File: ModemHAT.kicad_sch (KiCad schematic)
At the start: 99 parts, among them J1 RJ11, J2 2x20 0.1" Stacking Header, J3 8R, Q1 NPN 300V 0.5A, Q2 PNP 300V 0.5A, Q3 NPN 300V 0.5A, Q4 NPN 80V 330mW, Q5 NPN 80V 330mW, SW1 SW_SPDT, U1 Si2457-D-FT, U2 Si3018-F-GS, U3 74LVC541, U4 LM4819, U5 24LC32, U6 25LC320, Y1 32.768kHz 25ppm

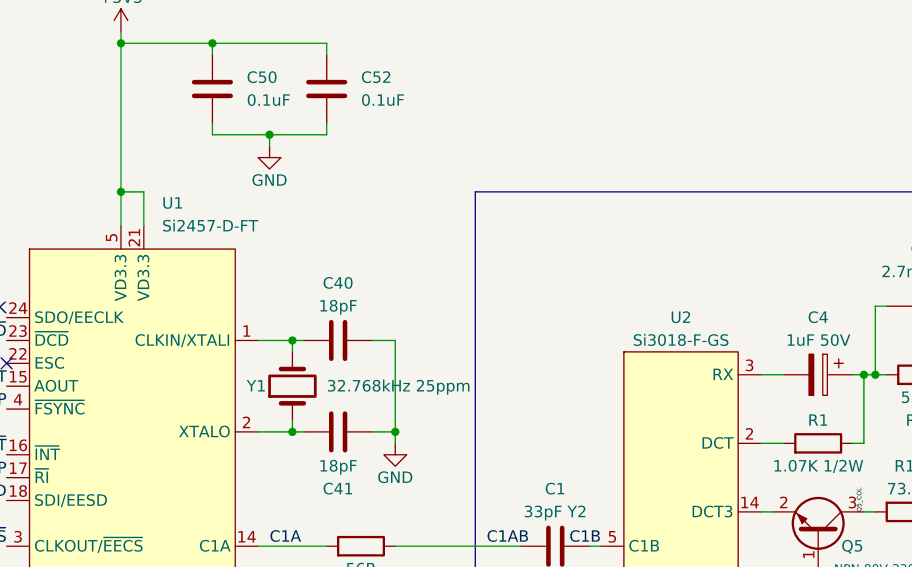
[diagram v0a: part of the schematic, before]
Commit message: added more mfg part numbers
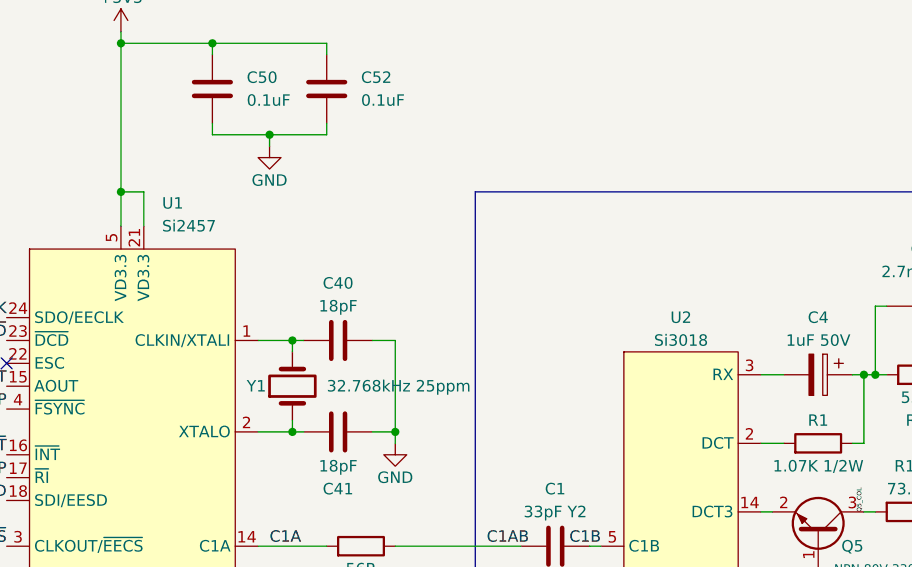
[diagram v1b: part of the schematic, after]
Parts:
- C3: MPN (none) -> GRM21BR72E103KW03L
- C8, C9: MPN (none) -> 502R29W681KV3E-****-SC
- D1: MPN MB4S -> MB4S-TP
- H1, H2, H3, H4: now left out of the parts list
- J1: MPN (none) -> 54601-906001WPLF
- SW1: MPN (none) -> JS102011SAQN
- U1: value Si2457-D-FT -> Si2457; MPN (none) -> Si2457-D-FT
- U2: value Si3018-F-GS -> Si3018; MPN (none) -> Si3018-F-GS
- U3: MPN (none) -> 74LVC541ABQ,115
- U4: MPN (none) -> LM4819MX/NOPB
- U5: MPN (none) -> CAT24C32YI-GT3
- U6: MPN (none) -> 25LC320AT-I/ST
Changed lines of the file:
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@@
+      (effects (font (size 1.27 1.27)) hide)
+    )
+    (property "MPN" "GRM21BR72E103KW03L" (id 4) (at 234.95 105.41 0)
       (effects (font (size 1.27 1.27)) hide)
     )
@@
   )
   (symbol (lib_id "Mechanical:MountingHole") (at 256.54 236.22 0) (unit 1)
-    (in_bom yes) (on_board yes) (fields_autoplaced)
+    (in_bom no) (on_board yes) (fields_autoplaced)
     (property "Reference" "H1" (id 0) (at 259.08 234.9499 0)
       (effects (font (size 1.27 1.27)) (justify left))
@@
   )
   (symbol (lib_id "Mechanical:MountingHole") (at 256.54 245.11 0) (unit 1)
-    (in_bom yes) (on_board yes) (fields_autoplaced)
+    (in_bom no) (on_board yes) (fields_autoplaced)
     (property "Reference" "H3" (id 0) (at 259.08 243.8399 0)
       (effects (font (size 1.27 1.27)) (justify left))
@@
     )
     (property "Datasheet" "~" (id 3) (at 262.89 142.24 0)
+      (effects (font (size 1.27 1.27)) hide)
+    )
+    (property "MPN" "502R29W681KV3E-****-SC" (id 4) (at 262.89 142.24 0)
       (effects (font (size 1.27 1.27)) hide)
     )
@@
     )
     (property "Datasheet" "~" (id 3) (at 298.45 90.805 90)
+      (effects (font (size 1.27 1.27)) hide)
+    )
+    (property "MPN" "54601-906001WPLF" (id 4) (at 298.45 90.17 0)
       (effects (font (size 1.27 1.27)) hide)
     )
@@
   )
   (symbol (lib_id "Graphic:Logo_Open_Hardware_Small") (at 397.51 261.62 0) (unit 1)
-    (in_bom yes) (on_board yes) (fields_autoplaced)
+    (in_bom no) (on_board yes) (fields_autoplaced)
     (property "Reference" "#LOGO1" (id 0) (at 397.51 254.635 0)
       (effects (font (size 1.27 1.27)) hide)
@@
       (effects (font (size 1.27 1.27)) hide)
     )
-    (property "MPN" "MB4S" (id 4) (at 237.49 90.17 0)
+    (property "MPN" "MB4S-TP" (id 4) (at 237.49 90.17 0)
       (effects (font (size 1.27 1.27)) hide)
     )
@@
   )
   (symbol (lib_id "Mechanical:MountingHole") (at 267.97 245.11 0) (unit 1)
-    (in_bom yes) (on_board yes) (fields_autoplaced)
+    (in_bom no) (on_board yes) (fields_autoplaced)
     (property "Reference" "H4" (id 0) (at 270.51 243.8399 0)
       (effects (font (size 1.27 1.27)) (justify left))
@@
       (effects (font (size 1.27 1.27)) (justify left))
     )
-    (property "Value" "Si2457-D-FT" (id 1) (at 79.4894 58.42 0)
+    (property "Value" "Si2457" (id 1) (at 79.4894 58.42 0)
       (effects (font (size 1.27 1.27)) (justify left))
     )
@@
     )
     (property "Datasheet" "" (id 3) (at 77.47 90.17 0)
+      (effects (font (size 1.27 1.27)) hide)
+    )
+    (property "MPN" "Si2457-D-FT" (id 4) (at 76.2 90.17 0)
       (effects (font (size 1.27 1.27)) hide)
     )
@@
       (effects (font (size 1.27 1.27)) hide)
     )
+    (property "MPN" "JS102011SAQN" (id 4) (at 195.58 243.84 0)
+      (effects (font (size 1.27 1.27)) hide)
+    )
     (pin "1")
     (pin "2")
@@
     )
     (property "Datasheet" "http://www.ti.com/lit/ds/symlink/lm4819.pdf" (id 3) (at 133.35 247.65 0)
+      (effects (font (size 1.27 1.27)) hide)
+    )
+    (property "MPN" "LM4819MX/NOPB" (id 4) (at 133.35 247.65 0)
       (effects (font (size 1.27 1.27)) hide)
     )
@@
     (in_bom yes) (on_board yes)
     (property "Reference" "U2" (id 0) (at 137.16 68.58 0))
-    (property "Value" "Si3018-F-GS" (id 1) (at 137.16 71.12 0))
+    (property "Value" "Si3018" (id 1) (at 137.16 71.12 0))
     (property "Footprint" "Package_SO:SOIC-16_3.9x9.9mm_P1.27mm" (id 2) (at 137.16 106.68 0)
       (effects (font (size 1.27 1.27)) hide)
     )
     (property "Datasheet" "" (id 3) (at 137.16 106.68 0)
+      (effects (font (size 1.27 1.27)) hide)
+    )
+    (property "MPN" "Si3018-F-GS" (id 4) (at 137.16 113.03 0)
       (effects (font (size 1.27 1.27)) hide)
     )
@@
   )
   (symbol (lib_id "Mechanical:MountingHole") (at 267.97 236.22 0) (unit 1)
-    (in_bom yes) (on_board yes) (fields_autoplaced)
+    (in_bom no) (on_board yes) (fields_autoplaced)
     (property "Reference" "H2" (id 0) (at 270.51 234.9499 0)
       (effects (font (size 1.27 1.27)) (justify left))
@@
     )
     (property "Datasheet" "~" (id 3) (at 269.24 142.24 0)
+      (effects (font (size 1.27 1.27)) hide)
+    )
+    (property "MPN" "502R29W681KV3E-****-SC" (id 4) (at 269.24 142.24 0)
       (effects (font (size 1.27 1.27)) hide)
     )
@@
       (effects (font (size 1.27 1.27)) hide)
     )
+    (property "MPN" "74LVC541ABQ,115" (id 4) (at 339.09 204.47 0)
+      (effects (font (size 1.27 1.27)) hide)
+    )
     (pin "1")
     (pin "10")
@@
       (effects (font (size 1.27 1.27)) hide)
     )
+    (property "MPN" "25LC320AT-I/ST" (id 4) (at 218.44 194.31 0)
+      (effects (font (size 1.27 1.27)) hide)
+    )
     (pin "1")
     (pin "2")
@@
       (effects (font (size 1.27 1.27)) hide)
     )
+    (property "MPN" "CAT24C32YI-GT3" (id 4) (at 361.95 128.27 0)
+      (effects (font (size 1.27 1.27)) hide)
+    )
     (pin "1")
     (pin "2")
@@
     )
     (path "/76561a30-8f21-41fc-a06c-445f9a92101b"
-      (reference "U1") (unit 1) (value "Si2457-D-FT") (footprint "Package_SO:TSSOP-24_4.4x7.8mm_P0.65mm")
+      (reference "U1") (unit 1) (value "Si2457") (footprint "Package_SO:TSSOP-24_4.4x7.8mm_P0.65mm")
     )
     (path "/9b33db79-b98e-4c51-8305-ed7f7bb70f13"
-      (reference "U2") (unit 1) (value "Si3018-F-GS") (footprint "Package_SO:SOIC-16_3.9x9.9mm_P1.27mm")
+      (reference "U2") (unit 1) (value "Si3018") (footprint "Package_SO:SOIC-16_3.9x9.9mm_P1.27mm")
     )
     (path "/f4f2738d-4efa-400b-bd93-c96242dafc30"

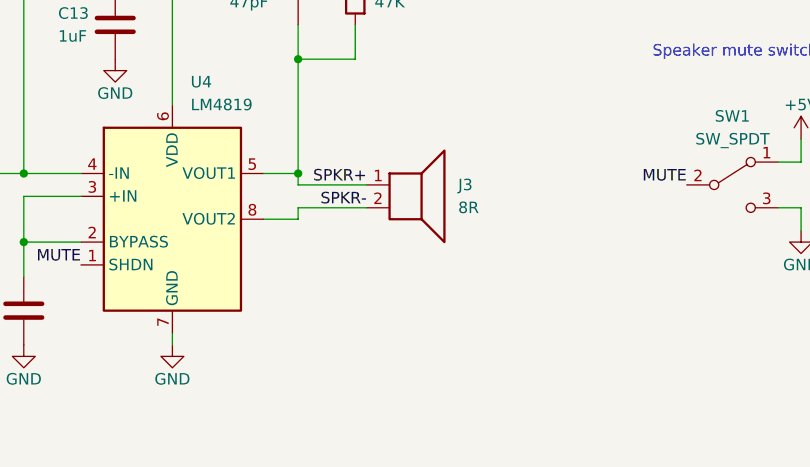
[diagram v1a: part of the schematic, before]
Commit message: audio circuit comments
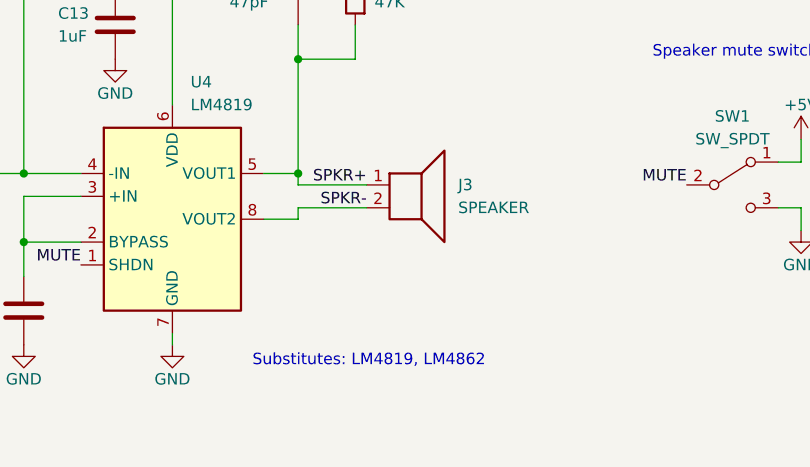
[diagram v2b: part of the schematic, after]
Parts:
- J3: value 8R -> SPEAKER
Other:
- note added: "Substitutes: LM4819, LM4862"
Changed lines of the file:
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@@
+    (effects (font (size 1.27 1.27)) (justify left bottom))
+  )
+  (text "Substitutes: LM4819, LM4862" (at 142.24 264.16 0)
     (effects (font (size 1.27 1.27)) (justify left bottom))
   )
@@
       (effects (font (size 1.27 1.27)) (justify left))
     )
-    (property "Value" "8R" (id 1) (at 165.1 246.3799 0)
+    (property "Value" "SPEAKER" (id 1) (at 165.1 246.3799 0)
       (effects (font (size 1.27 1.27)) (justify left))
     )
@@
     )
     (path "/6effeffe-d42d-4a4b-9f82-74cae02f5e28"
-      (reference "J3") (unit 1) (value "8R") (footprint "Connector_JST:JST_PH_B2B-PH-K_1x02_P2.00mm_Vertical")
+      (reference "J3") (unit 1) (value "SPEAKER") (footprint "Connector_JST:JST_PH_B2B-PH-K_1x02_P2.00mm_Vertical")
     )
     (path "/a1821338-ea80-47ff-948f-c44a9f05bfce"

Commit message: rev B
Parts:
- removed RN1, RN2: 470R, Resistor_SMD:R_Array_Concave_4x0603, symbol Device:R_Pack04_Split
- added LS1: Speaker, Buzzer_Beeper:Buzzer_15x7.5RM7.6, symbol Device:Speaker
- added R34, R35, R36, R37, R38, R39, R40, R41: 1K, Resistor_SMD:R_0603_1608Metric, symbol Device:R
- C10: LCSC (none) -> C57112
- C11, C14, C15, C16, C17, C18, C20, C22, C5, C50, C52, C56, C6: LCSC (none) -> C14663
- C12: LCSC (none) -> C1671
- C13, C19, C54: LCSC (none) -> C15849
- C21: LCSC (none) -> C14663; now not fitted
- C3: value 10nF 250V -> 0.01uF 250V
- C4: LCSC (none) -> C371267
- C40, C41: LCSC (none) -> C1647
- C51, C53: LCSC (none) -> C21120
- C7: LCSC (none) -> C1609
- D1: LCSC (none) -> C151727
- D2, D3, D4, D5, D6, D7, D8, D9: LCSC (none) -> C2297
- FB1, FB2, FB3: LCSC (none) -> C1002
- J1: footprint Connector_RJ:RJ12_Amphenol_54601 -> Connector_RJ:RJ12_Amphenol_54601-x06_Horizontal
- J2: LCSC (none) -> C2685112
- J3: value SPEAKER -> JST; symbol Device:Speaker -> Connector_Generic:Conn_01x02
- Q1, Q3: LCSC (none) -> C20069138
- Q2: LCSC (none) -> C20069146
- Q4, Q5: LCSC (none) -> C268584; MPN MMBTA06 -> MMBTA06W
- R1: footprint Resistor_SMD:R_2010_5025Metric -> Resistor_SMD:R_1210_3225Metric; LCSC (none) -> C333114
- R10: LCSC (none) -> C364152
- R11: footprint Resistor_SMD:R_2010_5025Metric -> Resistor_SMD:R_1210_3225Metric; LCSC (none) -> C2991291
- R12, R13: LCSC (none) -> C25196
- R14, R25: LCSC (none) -> C23018; now not fitted
- R15, R16: LCSC (none) -> C21189
- R17, R19, R23, R27, R28, R33: LCSC (none) -> C25804
- R18: value DNP -> 10K; LCSC (none) -> C25804; now not fitted
- R2: LCSC (none) -> C22808
- R20, R21, R22: LCSC (none) -> C21190
- R24: LCSC (none) -> C25819
- R26: value 200R -> 150R; LCSC (none) -> C22808
- R29, R30, R31, R32: value DNP -> 0R; LCSC (none) -> C25819; now not fitted
- R3: LCSC (none) -> C230230
- R4: footprint Resistor_SMD:R_1206_3216Metric -> Resistor_SMD:R_1210_3225Metric; LCSC (none) -> C705453
- R5, R6: LCSC (none) -> C25803
- R7, R8: LCSC (none) -> C384452
- R9: LCSC (none) -> C22935
- RV1: LCSC (none) -> C3012560
- SW1: footprint Button_Switch_SMD:SW_SPDT_CK-JS102011SAQN -> Button_Switch_SMD:SW_SPDT_CK_JS102011SAQN; LCSC (none) -> C221660
- U3: footprint Package_DFN_QFN:WQFN-20-1EP_2.5x4.5mm_P0.5mm_EP1x2.9mm -> Package_SO:TSSOP-20_4.4x6.5mm_P0.65mm; LCSC (none) -> C5657; MPN 74LVC541ABQ,115 -> (none)
- U4: LCSC (none) -> C87265
- U5: now not fitted
- U6: LCSC (none) -> C2061659
- Y1: LCSC (none) -> C32346
- Z1: LCSC (none) -> C6909653
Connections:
- net SPKR+: now also LS1.1
- net SPKR-: now also LS1.2
- net at D7.1 (K): now also R39.2
- net at D2.1 (K): now also R34.2
- net at D8.1 (K): now also R40.2
- net at D3.1 (K): now also R35.2
- net at U3.13 (Y5): now also R39.1
- net at U3.14 (Y4): now also R38.1
- net at D6.1 (K): now also R38.2
- net at D5.1 (K): now also R37.2
- net at U3.15 (Y3): now also R37.1
- net at U3.18 (Y0): now also R34.1
- net at U3.11 (Y7): now also R41.1
- net at D9.1 (K): now also R41.2
- net at U3.12 (Y6): now also R40.1
- net at U3.16 (Y2): now also R36.1
- net at D4.1 (K): now also R36.2
- net at U3.17 (Y1): now also R35.1
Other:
- company: ©2022 Adrian Studer -> ©2022-2024 Adrian Studer

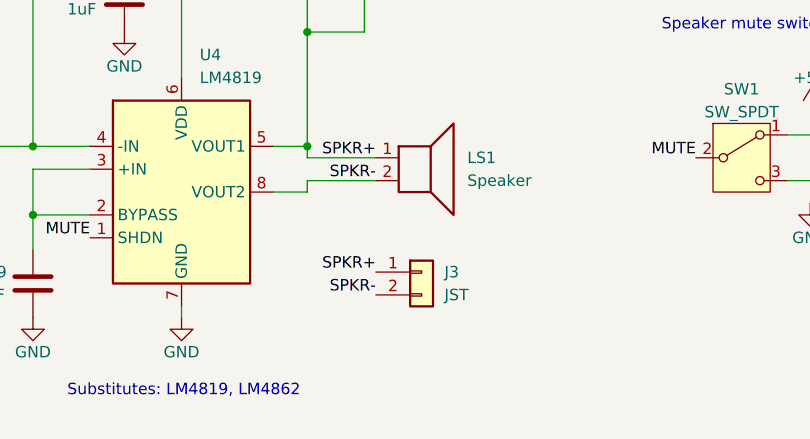
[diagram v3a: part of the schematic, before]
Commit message: add schematic PDF
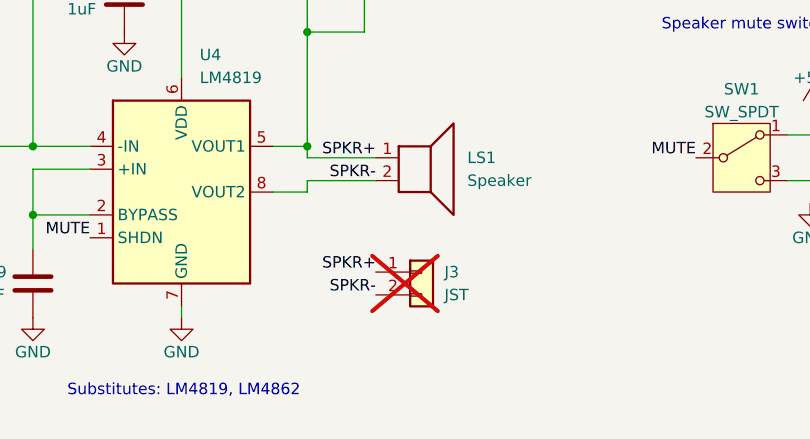
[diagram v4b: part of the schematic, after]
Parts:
- J3: now not fitted
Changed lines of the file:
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@@
 		(in_bom yes)
 		(on_board yes)
-		(dnp no)
+		(dnp yes)
 		(fields_autoplaced yes)
 		(property "Reference" "J3"
